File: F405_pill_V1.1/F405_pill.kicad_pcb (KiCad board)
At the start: 4 copper layers, 54.1 x 19.4 mm, 49 parts, among them J1 Conn_01x04_Male, J2 Conn_01x04_Male, J4 TYPE-C-31-M-12, U1 STM32F405RGTx, U2 TJA1050T/CM,118, U3 LM1117-3.3, U4 STM32F405_pill, U5 HT7550, Y1 Crystal_GND24

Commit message: add imu
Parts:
- added C23: 100n, Capacitor_SMD:C_0402_1005Metric, F.Cu at (105.8, 74.3)
- added C25: 100n, Capacitor_SMD:C_0402_1005Metric, F.Cu at (132.8, 71.5)
- added C27: 100n, Capacitor_SMD:C_0402_1005Metric, F.Cu at (105.8, 69.5)
- added C28: 100n, Capacitor_SMD:C_0402_1005Metric, F.Cu at (143.7, 71.0)
- added C29: 100n, Capacitor_SMD:C_0402_1005Metric, F.Cu at (142.1, 74.2)
- added C30: 100n, Capacitor_SMD:C_0402_1005Metric, F.Cu at (117.2, 74.3)
- added C31: 100n, Capacitor_SMD:C_0402_1005Metric, F.Cu at (117.4, 68.7)
- added C32: 100n, Capacitor_SMD:C_0402_1005Metric, F.Cu at (132.8, 73.7)
- added C33: 100n, Capacitor_SMD:C_0402_1005Metric, F.Cu at (120.0, 71.7)
- added C34: 100n, Capacitor_SMD:C_0402_1005Metric, F.Cu at (129.2, 74.3)
- added J5: Conn_01x02, Connector_PinHeader_2.54mm:PinHeader_1x02_P2.54mm_Vertical, F.Cu at (98.3, 70.4)
- added JP10: SCL, Jumper:SolderJumper-2_P1.3mm_Open_RoundedPad1.0x1.5mm, F.Cu at (124.8, 70.5)
- added JP3: SDA, Jumper:SolderJumper-2_P1.3mm_Open_RoundedPad1.0x1.5mm, F.Cu at (102.2, 73.1)
- added JP4: SCL, Jumper:SolderJumper-2_P1.3mm_Open_RoundedPad1.0x1.5mm, F.Cu at (102.2, 70.5)
- added JP5: SDA, Jumper:SolderJumper-2_P1.3mm_Open_RoundedPad1.0x1.5mm, F.Cu at (136.5, 73.1)
- added JP6: SCL, Jumper:SolderJumper-2_P1.3mm_Open_RoundedPad1.0x1.5mm, F.Cu at (136.5, 70.5)
- added JP7: SDA, Jumper:SolderJumper-2_P1.3mm_Open_RoundedPad1.0x1.5mm, F.Cu at (112.3, 73.1)
- added JP8: SCL, Jumper:SolderJumper-2_P1.3mm_Open_RoundedPad1.0x1.5mm, F.Cu at (112.3, 70.5)
- added JP9: SDA, Jumper:SolderJumper-2_P1.3mm_Open_RoundedPad1.0x1.5mm, F.Cu at (124.8, 73.0)
- added R13: 2.4K, Resistor_SMD:R_0805_2012Metric, F.Cu at (109.5, 69.7)
- added R14: 2.4K, Resistor_SMD:R_0805_2012Metric, F.Cu at (109.5, 73.1)
- added U6: BMI160, Package_LGA:Bosch_LGA-14_3x2.5mm_P0.5mm, F.Cu at (106.2, 72.0)
- added U7: MPU-9250, Sensor_Motion:InvenSense_QFN-24_3x3mm_P0.4mm, F.Cu at (129.7, 71.5)
- added U8: LSM6DS3, Package_LGA:LGA-14_3x2.5mm_P0.5mm_LayoutBorder3x4y, F.Cu at (141.4, 71.9)
- added U9: ICM-20948, Sensor_Motion:InvenSense_QFN-24_3x3mm_P0.4mm, F.Cu at (117.2, 71.6)
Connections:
- U1 pad 29: DUAL1 -> PB10
- U1 pad 30: DUAL2 -> PB11
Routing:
- net PB10: track 0.00 -> 56.1 mm, vias 0 -> 5
- net PB11: track 0.00 -> 49.8 mm, vias 0 -> 6
- net GND: track 69.1 -> 104.0 mm, vias 89 -> 103
- net DUAL2: track 24.8 -> 4.07 mm, vias 1 -> 0
- net DUAL1: track 23.8 -> 5.29 mm, vias 1 -> 0
- net Net-(JP4-B): track 0.00 -> 5.58 mm
- net Net-(U9-VDDIO): track 0.00 -> 5.31 mm
- net Net-(U7-VDDIO): track 0.00 -> 5.15 mm
- net Net-(JP9-B): track 0.00 -> 4.71 mm
- net Net-(JP7-B): track 0.00 -> 4.70 mm
- net Net-(JP3-B): track 0.00 -> 4.63 mm
- net Net-(JP10-B): track 0.00 -> 4.34 mm
- net Net-(JP8-B): track 0.00 -> 4.32 mm
- net Net-(JP6-B): track 0.00 -> 4.10 mm
- net Net-(JP5-B): track 0.00 -> 3.62 mm
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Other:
- board size 54.1 x 19.4 mm -> 54.1 x 26.6 mm

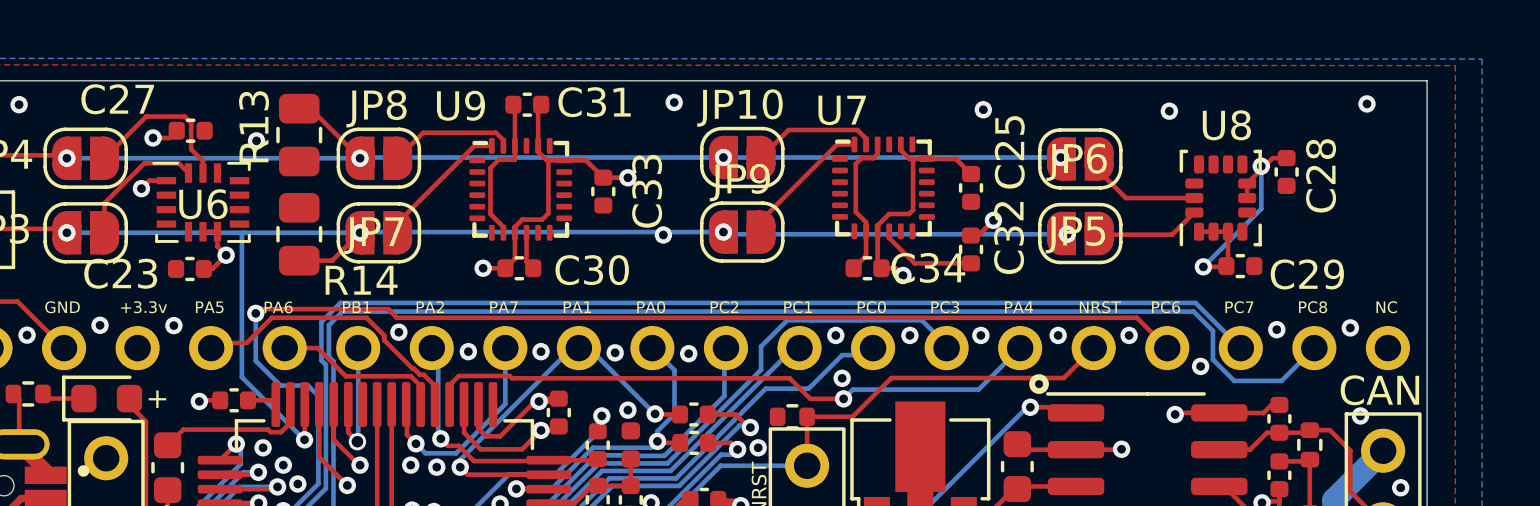
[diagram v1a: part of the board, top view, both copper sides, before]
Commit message: add bmi270
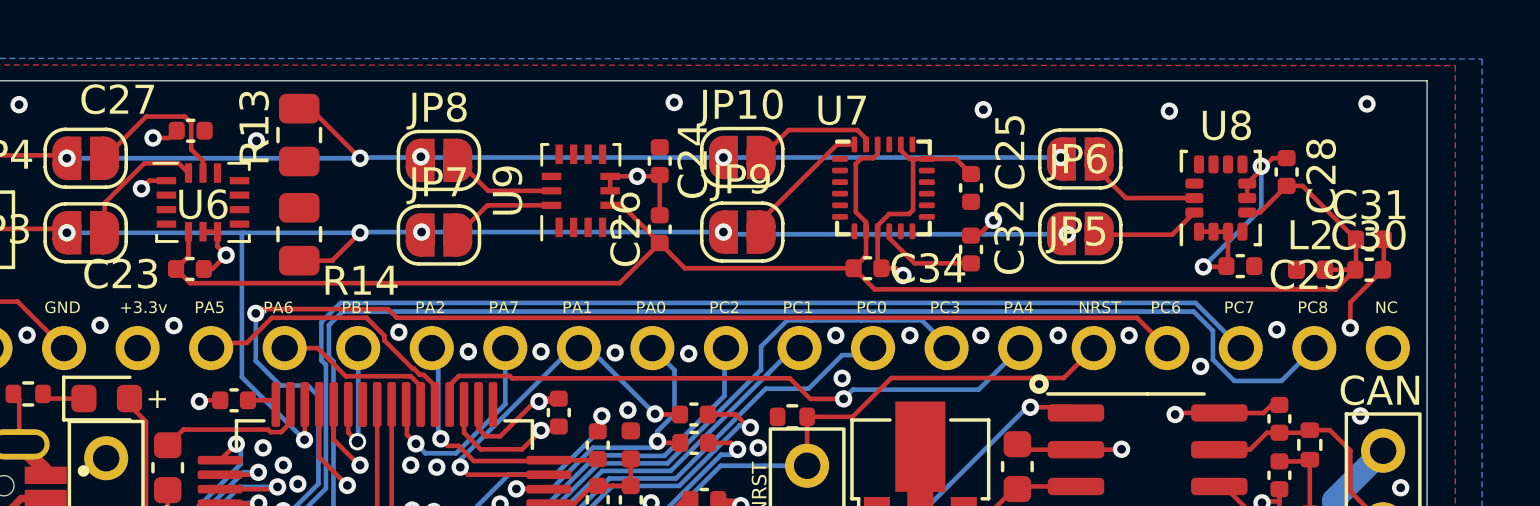
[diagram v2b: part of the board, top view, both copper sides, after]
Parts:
- removed C33: 100n, Capacitor_SMD:C_0402_1005Metric
- added C24: 100n, Capacitor_SMD:C_0402_1005Metric, F.Cu at (122.0, 70.6)
- added C26: 100n, Capacitor_SMD:C_0402_1005Metric, F.Cu at (122.0, 73.0)
- added L2: 39n, Inductor_SMD:L_0402_1005Metric, F.Cu at (144.5, 74.3)
- C30: value 100n -> 1u
- C31: value 100n -> 10n
- U9: value ICM-20948 -> BMI270; footprint Sensor_Motion:InvenSense_QFN-24_3x3mm_P0.4mm -> Package_LGA:Bosch_LGA-14_3x2.5mm_P0.5mm
- moved C31 29.5 mm to (146.5, 73.3), turned to 0 degrees
- moved C30 29.4 mm to (146.5, 74.3), turned to 0 degrees
- moved JP7 2.08 mm to (114.4, 73.2)
- moved JP8 2.08 mm to (114.4, 70.6)
- moved U9 2.08 mm to (119.3, 71.6), turned to 90 degrees
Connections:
- C23 pad 1: +3V3 -> 3.3F
- C28 pad 1: +3V3 -> 3.3F
- C30 pad 1: Net-(U9-REGOUT) -> 3.3F
- C31 pad 1: GND -> 3.3F
- C31 pad 2: Net-(U9-VDDIO) -> GND
- C34 pad 2: Net-(U7-VDDIO) -> 3.3F
- U6 pad 5: +3V3 -> 3.3F
- U7 pad 22: Net-(U7-VDDIO) -> 3.3F
- U7 pad 8: Net-(U7-VDDIO) -> 3.3F
- U8 pad 5: +3V3 -> 3.3F
- U9 pad 1: unconnected-(U9-NC-Pad1) -> +3V3
- U9 pad 10: Net-(U9-REGOUT) -> unconnected-(U9-OCSB-Pad10)
- U9 pad 12: unconnected-(U9-INT1-Pad12) -> +3V3
- U9 pad 13: +3V3 -> Net-(JP8-B)
- U9 pad 14: unconnected-(U9-NC-Pad14) -> Net-(JP7-B)
- U9 pad 5: unconnected-(U9-NC-Pad5) -> 3.3F
- U9 pad 6: unconnected-(U9-NC-Pad6) -> GND
- U9 pad 7: unconnected-(U9-AUX_CL-Pad7) -> GND
- U9 pad 8: Net-(U9-VDDIO) -> +3V3
- U9 pad 9: GND -> unconnected-(U9-INT2-Pad9)
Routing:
- net 3.3F: track 0.00 -> 58.3 mm
- net Net-(U9-VDDIO): track 5.31 -> 0.00 mm
- net Net-(U7-VDDIO): track 5.15 -> 0.00 mm
- net GND: track 104.0 -> 100.5 mm, vias 103 -> 102
- net Net-(U9-REGOUT): track 1.32 -> 0.00 mm
- net Net-(JP7-B): track 4.70 -> 3.66 mm
- net Net-(JP8-B): track 4.32 -> 3.67 mm
- net PB10: vias 5 -> 6

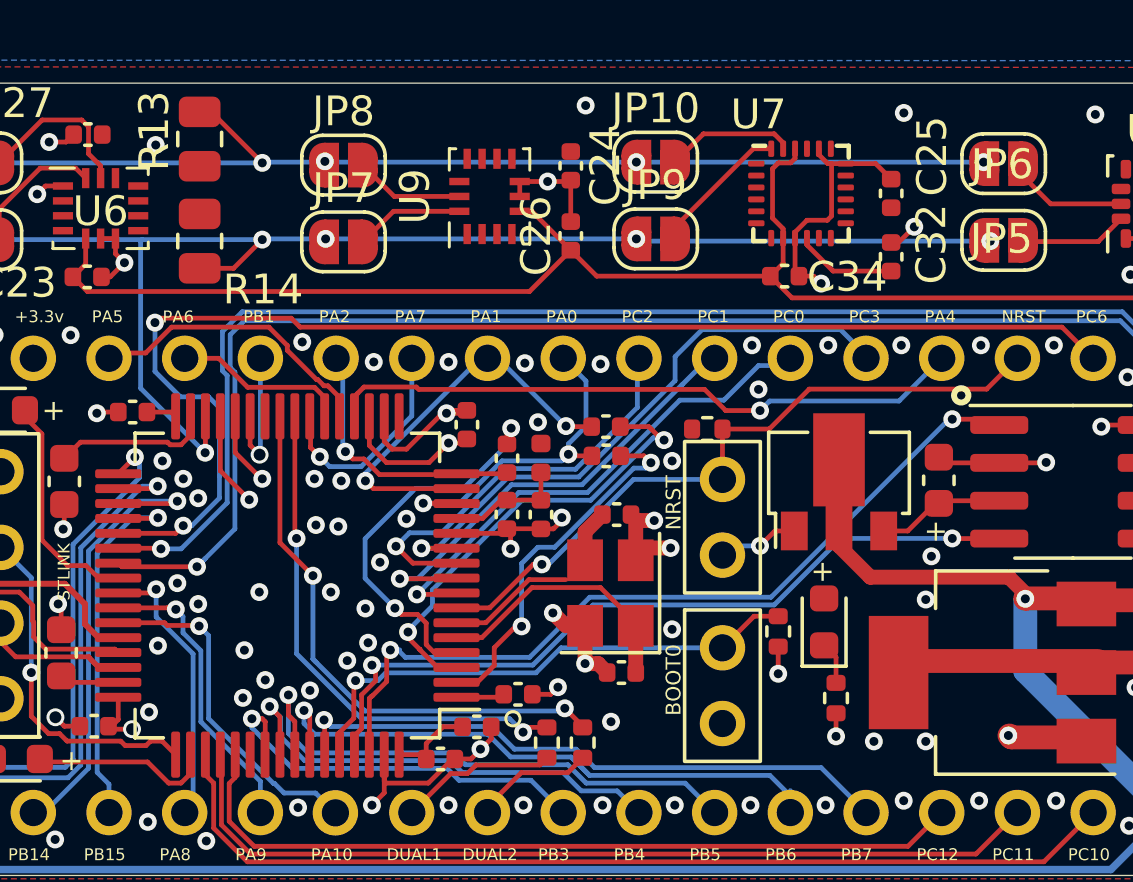
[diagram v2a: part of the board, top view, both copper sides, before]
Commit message: fixed for prodaction
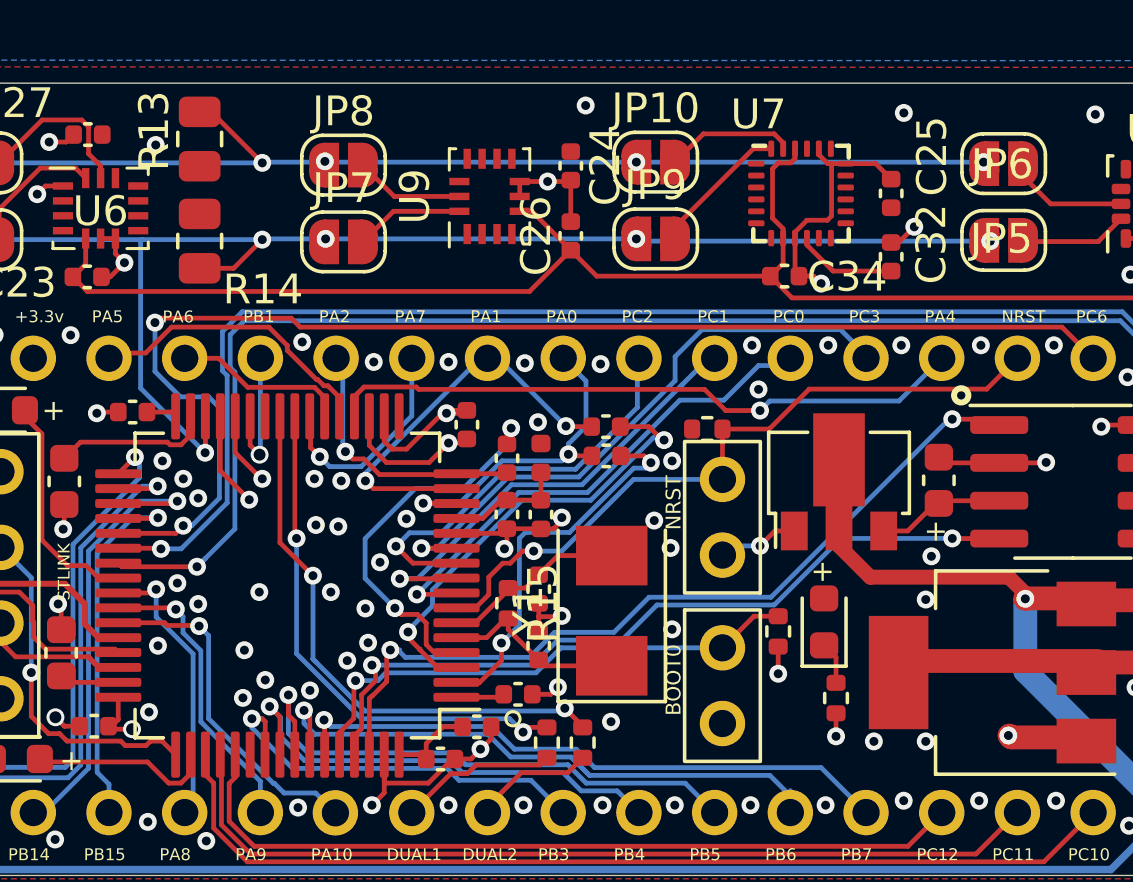
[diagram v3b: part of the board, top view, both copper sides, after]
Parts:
- added R15: 1M, Resistor_SMD:R_0402_1005Metric, F.Cu at (119.9, 85.3)
- C3, C6: value 12p -> 20pF
- Y1: value Crystal_GND24 -> 8MHz; footprint Crystal:Crystal_SMD_3225-4Pin_3.2x2.5mm -> Crystal:Crystal_SMD_5032-2Pin_5.0x3.2mm
- moved C6 3.62 mm to (120.9, 84.8), turned to 90 degrees
- moved C3 2.92 mm to (120.9, 86.7), turned to -90 degrees
- moved Y1 0.59 mm to (123.4, 85.5)
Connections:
- C3 pad 1: Net-(U1-PH0) -> GND
- C3 pad 2: GND -> Net-(U1-PH0)
- C6 pad 1: Net-(U1-PH1) -> GND
- C6 pad 2: GND -> Net-(U1-PH1)
- Y1 pad 2: GND -> Net-(U1-PH1)
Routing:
- net GND: track 100.5 -> 95.0 mm, vias 102 -> 100
- net Net-(U1-PH0): track 8.67 -> 7.21 mm
- net Net-(U1-PH1): track 6.04 -> 6.18 mm, vias 0 -> 1

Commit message: add MCU
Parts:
- removed C23, C24, C25, C26, C27, C32, C34: 100n, Capacitor_SMD:C_0402_1005Metric
- removed JP10, JP4, JP6, JP8: SCL, Jumper:SolderJumper-2_P1.3mm_Open_RoundedPad1.0x1.5mm
- removed JP3, JP5, JP7, JP9: SDA, Jumper:SolderJumper-2_P1.3mm_Open_RoundedPad1.0x1.5mm
- removed U6: BMI160, Package_LGA:Bosch_LGA-14_3x2.5mm_P0.5mm
- removed U7: MPU-9250, Sensor_Motion:InvenSense_QFN-24_3x3mm_P0.4mm
- removed U9: BMI270, Package_LGA:Bosch_LGA-14_3x2.5mm_P0.5mm
- U1: value STM32F405RGTx -> STM32F405VGTx; footprint Package_QFP:LQFP-64_10x10mm_P0.5mm -> Package_QFP:LQFP-100_14x14mm_P0.5mm
- U2: value TJA1050T/CM,118 -> TJA1050T/CM,118
- moved C18 41.9 mm to (81.4, 75.4), turned to -90 degrees
- moved C17 41.0 mm to (82.5, 75.4), turned to -90 degrees
- moved C19 39.8 mm to (80.3, 75.4)
- moved C5 38.2 mm to (83.9, 73.2), turned to 180 degrees
- moved C12 37.7 mm to (80.2, 86.1), turned to 90 degrees
- moved C8 37.3 mm to (83.9, 72.1), turned to 180 degrees
- moved R5 37.1 mm to (132.4, 70.9), turned to 180 degrees
- moved L1 35.9 mm to (85.8, 73.2), turned to 180 degrees
- moved Y1 35.4 mm to (90.1, 73.4), turned to 180 degrees
- moved C6 34.7 mm to (89.1, 70.9), turned to 180 degrees
- moved C3 33.7 mm to (91.1, 70.9), turned to 0 degrees
- moved R15 33.5 mm to (90.1, 69.9), turned to 0 degrees
- moved D2 32.9 mm to (129.8, 70.9), turned to 180 degrees
- moved C4 32.9 mm to (86.0, 74.4), turned to 180 degrees
- moved R7 32.8 mm to (132.4, 72.7), turned to 180 degrees
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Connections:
- U1 pad 1: +3V3 -> unconnected-(U1-PE2-Pad1)
- U1 pad 10: PC2 -> GND
- U1 pad 11: PC3 -> +3V3
- U1 pad 12: GND -> Net-(U1-PH0)
- U1 pad 13: +3.3VA -> Net-(U1-PH1)
- U1 pad 14: PA0 -> NRST
- U1 pad 15: PA1 -> PC0
- U1 pad 16: PA2 -> PC1
- U1 pad 17: PA3 -> PC2
- U1 pad 18: GND -> PC3
- U1 pad 2: PC13 -> unconnected-(U1-PE3-Pad2)
- U1 pad 20: PA4 -> GND
- U1 pad 21: PA5 -> +3.3VA
- U1 pad 22: PA6 -> +3.3VA
- U1 pad 23: PA7 -> PA0
- U1 pad 24: PC4 -> PA1
- U1 pad 25: PC5 -> PA2
- U1 pad 26: PB0 -> PA3
- U1 pad 27: PB1 -> GND
- U1 pad 28: GND -> +3V3
- U1 pad 29: PB10 -> PA4
- U1 pad 3: PC14 -> unconnected-(U1-PE4-Pad3)
- U1 pad 30: PB11 -> PA5
- U1 pad 31: Net-(U1-VCAP_1) -> PA6
- U1 pad 32: +3V3 -> PA7
- U1 pad 33: PB12 -> PC4
- U1 pad 34: PB13 -> PC5
- U1 pad 35: PB14 -> PB0
- U1 pad 36: PB15 -> PB1
- U1 pad 37: PC6 -> GND
- U1 pad 38: PC7 -> unconnected-(U1-PE7-Pad38)
- U1 pad 39: PC8 -> unconnected-(U1-PE8-Pad39)
- U1 pad 4: PC15 -> unconnected-(U1-PE5-Pad4)
- U1 pad 40: PC9 -> unconnected-(U1-PE9-Pad40)
- U1 pad 41: PA8 -> unconnected-(U1-PE10-Pad41)
- U1 pad 42: PA9 -> unconnected-(U1-PE11-Pad42)
- U1 pad 43: PA10 -> unconnected-(U1-PE12-Pad43)
- U1 pad 44: USB_D- -> unconnected-(U1-PE13-Pad44)
- U1 pad 45: USB_D+ -> unconnected-(U1-PE14-Pad45)
- U1 pad 46: SWDIO -> unconnected-(U1-PE15-Pad46)
- U1 pad 47: Net-(U1-VCAP_2) -> PB10
- U1 pad 48: +3V3 -> PB11
- U1 pad 49: SWCLK -> Net-(U1-VCAP_1)
- U1 pad 5: Net-(U1-PH0) -> unconnected-(U1-PE6-Pad5)
- U1 pad 50: PA15 -> +3V3
- U1 pad 51: PC10 -> PB12
- U1 pad 52: PC11 -> PB13
- U1 pad 53: PC12 -> PB14
- U1 pad 54: PD2 -> PB15
- U1 pad 55: PB3 -> unconnected-(U1-PD8-Pad55)
- U1 pad 56: PB4 -> unconnected-(U1-PD9-Pad56)
- U1 pad 57: PB5 -> unconnected-(U1-PD10-Pad57)
- U1 pad 58: PB6 -> unconnected-(U1-PD11-Pad58)
- U1 pad 59: PB7 -> unconnected-(U1-PD12-Pad59)
- U1 pad 6: Net-(U1-PH1) -> +3V3
- U1 pad 60: Net-(JP1-B) -> unconnected-(U1-PD13-Pad60)
- U1 pad 61: PB8 -> unconnected-(U1-PD14-Pad61)
- U1 pad 62: PB9 -> unconnected-(U1-PD15-Pad62)
- U1 pad 63: GND -> PC6
- U1 pad 64: +3V3 -> PC7
- U1 pad 7: NRST -> PC13
- U1 pad 8: PC0 -> PC14
- U1 pad 9: PC1 -> PC15
- U8 pad 13: Net-(JP6-B) -> PB10
- U8 pad 14: Net-(JP5-B) -> PB11
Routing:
- net GND: track 95.0 -> 0.00 mm, vias 100 -> 0
- net +5V: track 94.2 -> 0.00 mm, vias 4 -> 0
- net 3.3F: track 58.3 -> 0.00 mm
- net PB10: track 56.1 -> 0.00 mm, vias 6 -> 0
- net PB11: track 49.8 -> 0.00 mm, vias 6 -> 0
- net PC8: track 47.6 -> 0.00 mm, vias 1 -> 0
- net PC6: track 43.3 -> 0.00 mm, vias 2 -> 0
- net PC7: track 42.8 -> 0.00 mm, vias 1 -> 0
- net PC10: track 33.2 -> 0.00 mm
- net PC11: track 30.1 -> 0.00 mm
- net +3V3: track 29.9 -> 0.00 mm, vias 12 -> 1
- net PB9: track 27.8 -> 0.00 mm, vias 2 -> 0
- net PC12: track 27.0 -> 0.00 mm
- net PB8: track 26.2 -> 0.00 mm, vias 2 -> 0
- net NRST: track 23.6 -> 0.00 mm, vias 1 -> 0
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- removed copper zone on B.Cu, net +3V3
- removed copper zone on F.Cu, net +3V3
- removed copper zone on In1.Cu, net GND
- removed copper zone on In2.Cu, net GND
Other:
- board size 54.1 x 26.6 mm -> 69.5 x 26.6 mm
- board text added: "STM32F405VG PILL V1.2"
- board text removed: "+"
- board text removed: "+5v"
- board text removed: "3V3"
- board text removed: "BOOT0"
- board text removed: "CAN_H"
- board text removed: "CAN_L"
- board text removed: "LICENSE: BSD"
- board text removed: "STLINK"
- board text removed: "STM32F405RG PILL V1.1"
- board text removed: "SWCLK"
- board text removed: "SWDIO"

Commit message: Schematic is finished
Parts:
- added C23: 4u7, Capacitor_SMD:C_0402_1005Metric, F.Cu at (91.2, 68.5)
- added J3: Conn_01x04_Male, Connector_PinHeader_2.54mm:PinHeader_1x04_P2.54mm_Vertical, F.Cu at (138.1, 71.0)
- added R16: 100Ω, Resistor_SMD:R_0402_1005Metric, F.Cu at (101.8, 84.2)
- added R17: 100Ω, Resistor_SMD:R_0402_1005Metric, F.Cu at (103.2, 84.2)
- added U6: E73-2G4M08S1C, CCC_ESC_Custom_parts:E73-2G4M08S1C, B.Cu at (88.8, 79.2)
- moved R8 8.30 mm to (116.5, 90.0)
- moved R12 7.45 mm to (119.2, 90.3)
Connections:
- net PA0 renamed A_PHA_VSENSE
- net PA1 renamed A_PHB_VSENSE
- net PA10 renamed HIN_C
- net PA2 renamed A_PHC_VSENSE
- net PA4 renamed A_THROTTLE
- net PA8 renamed HIN_A
- net PA9 renamed HIN_B
- net PB1 renamed FET_TEMP
- net PB10 renamed I2C_SCL
- net PB11 renamed I2C_SDA
- net PB13 renamed LIN_A
- net PB14 renamed LIN_B
- net PB15 renamed LIN_C
- net PC0 renamed A_SHA_AMP
- net PC1 renamed A_SHB_AMP
- net PC2 renamed A_SHC_AMP
- net PC3 renamed VSENSE
- net PC6 renamed HALL_C
- net PC7 renamed HALL_B
- net PC8 renamed HALL_A
- net _PB12 renamed A_OVERLIMIT
- U1 pad 85: unconnected-(U1-PD4-Pad85) -> /NRF/TX
- U1 pad 86: unconnected-(U1-PD5-Pad86) -> /NRF/RX

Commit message: Rarticly routed
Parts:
- moved C12 5.71 mm to (81.0, 91.8), turned to -90 degrees
- moved U6 5.47 mm to (88.9, 73.8), turned to 180 degrees
- moved C9 3.17 mm to (80.0, 85.8)
- moved R12 1.47 mm to (117.9, 90.8)
- moved R8 1.38 mm to (115.5, 90.9)
- moved C17 0.98 mm to (83.2, 74.8), turned to 180 degrees
- moved C23 0.35 mm to (91.0, 68.8)
- turned C16 to 90 degrees
- turned C18 to 90 degrees
- turned R10 to -90 degrees
- turned R13 to -90 degrees
- turned R14 to -90 degrees
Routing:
- net +3V3: track 0.00 -> 70.4 mm, vias 1 -> 9
- net PB8: track 0.00 -> 46.4 mm, vias 0 -> 2
- net +5V: track 0.00 -> 40.3 mm
- net PB9: track 0.00 -> 39.5 mm, vias 0 -> 2
- net I2C_SCL: track 0.00 -> 37.2 mm, vias 0 -> 1
- net I2C_SDA: track 0.00 -> 36.4 mm, vias 0 -> 1
- net GND: track 0.00 -> 36.3 mm
- net PB4: track 0.00 -> 31.9 mm
- net PB3: track 0.00 -> 30.5 mm
- net HIN_C: track 0.00 -> 30.0 mm, vias 0 -> 1
- net SWDIO: track 0.00 -> 27.3 mm, vias 0 -> 1
- net HIN_B: track 0.00 -> 26.2 mm, vias 0 -> 1
- net LIN_C: track 0.00 -> 23.5 mm, vias 0 -> 1
- net HIN_A: track 0.00 -> 22.5 mm, vias 0 -> 1
- net LIN_B: track 0.00 -> 21.8 mm, vias 0 -> 1
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- added copper zone on In1.Cu, net +3V3
- added copper zone on In2.Cu, net +3V3
- added copper zone on B.Cu, net GND
- added copper zone on F.Cu, net GND

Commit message: pcb finished
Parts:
- moved R12 39.0 mm to (79.8, 82.6), turned to 0 degrees
- moved R8 37.1 mm to (79.8, 80.7), turned to 0 degrees
- moved C18 1.65 mm to (80.0, 76.2), turned to -90 degrees
- moved C19 1.20 mm to (81.5, 75.2)
- moved C2 0.51 mm to (100.3, 79.1)
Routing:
- net PC9: track 0.00 -> 70.4 mm, vias 0 -> 2
- net A_THROTTLE: track 0.00 -> 68.8 mm, vias 0 -> 1
- net Net-(J3-Pin_3): track 0.00 -> 68.7 mm, vias 0 -> 1
- net Net-(J3-Pin_2): track 0.00 -> 63.9 mm, vias 0 -> 1
- net HALL_A: track 0.00 -> 61.8 mm, vias 0 -> 1
- net HALL_B: track 0.00 -> 61.1 mm, vias 0 -> 1
- net HALL_C: track 0.00 -> 60.5 mm, vias 0 -> 1
- net PA15: track 0.00 -> 59.0 mm, vias 0 -> 2
- net A_SHA_AMP: track 0.00 -> 53.6 mm
- net VSENSE: track 0.00 -> 52.7 mm, vias 0 -> 1
- net A_PHA_VSENSE: track 2.08 -> 52.3 mm, vias 0 -> 1
- net A_PHB_VSENSE: track 3.78 -> 53.3 mm, vias 0 -> 1
- net PC10: track 0.00 -> 47.9 mm, vias 0 -> 1
- net PC11: track 0.00 -> 47.8 mm
- net NRST: track 15.8 -> 62.7 mm
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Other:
- board size 69.5 x 26.6 mm -> 70.5 x 26.6 mm
